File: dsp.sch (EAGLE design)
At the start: 128 parts, among them IC1 OPA2134P, IC2 OPA2134P, IC3 OPA2134P, U1 STM32F405RGT6, U2 CODECODER-WM8731SEDS/V(SSOP28), U4 LM2575HVS-3.3/NOPB, X1 ABLS-8.000MHZ-B4-T

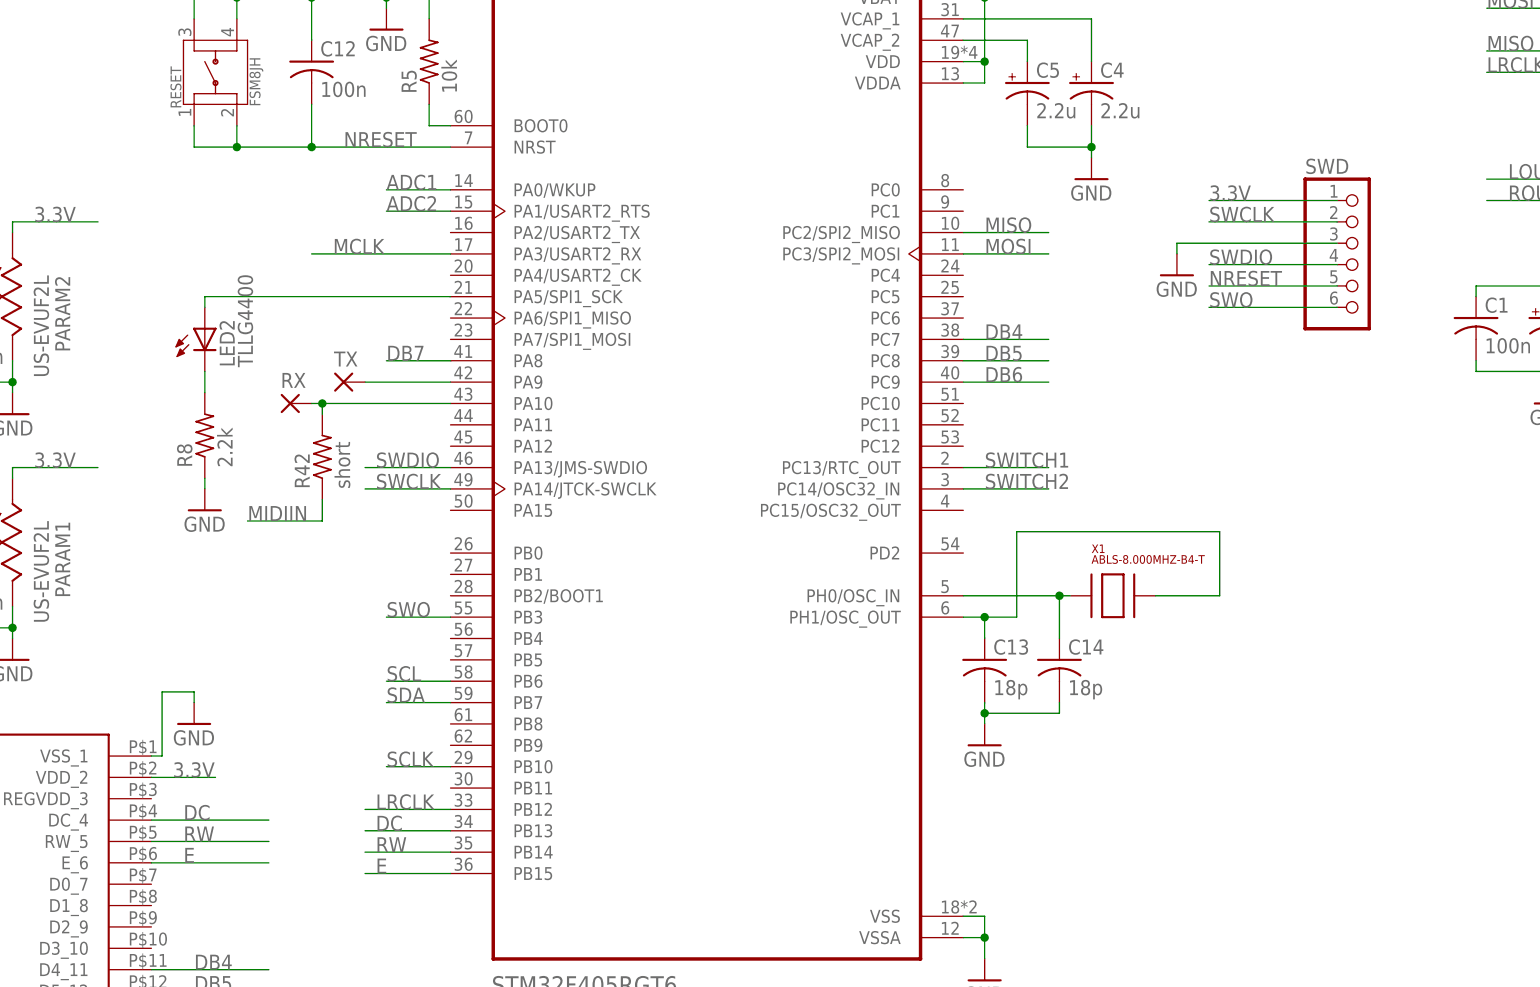
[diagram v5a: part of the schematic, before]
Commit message: added a ground for vccref and moved icp header to edge
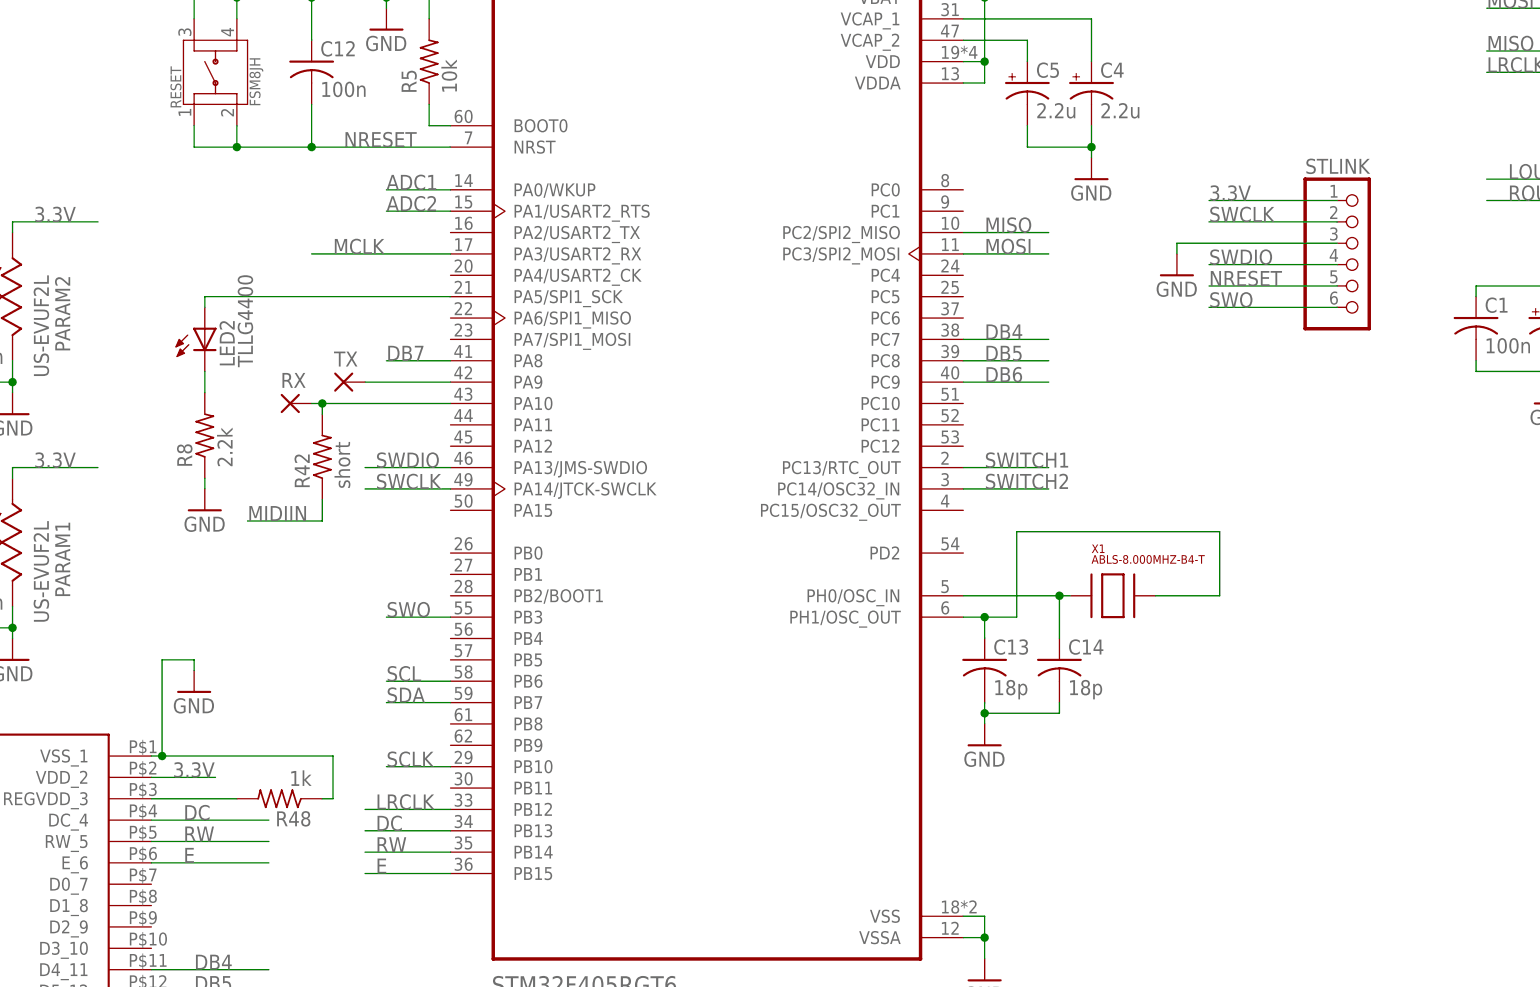
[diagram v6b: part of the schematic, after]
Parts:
- added R48: 1k, dan:R-US_0309/V
- renumbered SWD to STLINK
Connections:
- new net N$59: R48.2, U$1.REGVDD_3
- net GND: now also R48.1
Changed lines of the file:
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@@
 <part name="C28" library="dan" deviceset="C-US" device="050-025X075" value="180p"/>
 <part name="C29" library="dan" deviceset="C-US" device="050-025X075" value="180p"/>
-<part name="SWD" library="dan" deviceset="PINHD-1X6" device=""/>
+<part name="STLINK" library="dan" deviceset="PINHD-1X6" device=""/>
 <part name="RX" library="synthdiy" deviceset="2,0/0,9-S" device=""/>
 <part name="TX" library="synthdiy" deviceset="2,0/0,9-S" device=""/>
@@
 <part name="C37" library="dan" deviceset="CPOL-US" device="E2-4" value="1u"/>
 <part name="GND30" library="dan" deviceset="GND" device=""/>
+<part name="R48" library="dan" deviceset="R-US_" device="0309/V" value="1k"/>
 </parts>
 <sheets>
@@
 <instance part="R22" gate="G$1" x="99.06" y="212.09" rot="R90"/>
 <instance part="D4" gate="G$1" x="60.96" y="212.09" rot="R90"/>
-<instance part="GND35" gate="1" x="-7.62" y="10.16"/>
+<instance part="GND35" gate="1" x="-7.62" y="13.97"/>
 <instance part="GND36" gate="1" x="3.81" y="-33.02"/>
 <instance part="GND37" gate="1" x="-11.43" y="-45.72"/>
@@
 <instance part="C28" gate="G$1" x="295.91" y="118.11" rot="R90"/>
 <instance part="C29" gate="G$1" x="293.37" y="181.61" rot="R90"/>
-<instance part="SWD" gate="A" x="130.81" y="64.77"/>
+<instance part="STLINK" gate="A" x="130.81" y="64.77"/>
 <instance part="RX" gate="P" x="3.81" y="48.26"/>
 <instance part="TX" gate="P" x="10.16" y="50.8"/>
@@
 <instance part="C37" gate="G$1" x="209.55" y="67.31"/>
 <instance part="GND30" gate="1" x="203.2" y="83.82"/>
+<instance part="R48" gate="G$1" x="2.54" y="1.27" rot="R180"/>
 </instances>
 <busses>
@@
 <wire x1="109.22" y1="67.31" x2="109.22" y2="66.04" width="0.1524" layer="91"/>
 <pinref part="GND26" gate="1" pin="GND"/>
-<pinref part="SWD" gate="A" pin="3"/>
+<pinref part="STLINK" gate="A" pin="3"/>
 </segment>
 <segment>
@@
 <pinref part="U$1" gate="G$1" pin="VSS_1"/>
 <wire x1="-12.7" y1="6.35" x2="-11.43" y2="6.35" width="0.1524" layer="91"/>
-<wire x1="-11.43" y1="6.35" x2="-11.43" y2="13.97" width="0.1524" layer="91"/>
+<wire x1="-11.43" y1="6.35" x2="-11.43" y2="17.78" width="0.1524" layer="91"/>
 <pinref part="GND35" gate="1" pin="GND"/>
-<wire x1="-11.43" y1="13.97" x2="-7.62" y2="13.97" width="0.1524" layer="91"/>
-<wire x1="-7.62" y1="13.97" x2="-7.62" y2="12.7" width="0.1524" layer="91"/>
+<wire x1="-11.43" y1="17.78" x2="-7.62" y2="17.78" width="0.1524" layer="91"/>
+<wire x1="-7.62" y1="17.78" x2="-7.62" y2="16.51" width="0.1524" layer="91"/>
+<pinref part="R48" gate="G$1" pin="1"/>
+<wire x1="7.62" y1="1.27" x2="8.89" y2="1.27" width="0.1524" layer="91"/>
+<wire x1="8.89" y1="1.27" x2="8.89" y2="6.35" width="0.1524" layer="91"/>
+<wire x1="8.89" y1="6.35" x2="-11.43" y2="6.35" width="0.1524" layer="91"/>
+<junction x="-11.43" y="6.35"/>
 </segment>
 <segment>
@@
 </segment>
 <segment>
-<pinref part="SWD" gate="A" pin="1"/>
+<pinref part="STLINK" gate="A" pin="1"/>
 <wire x1="128.27" y1="72.39" x2="113.03" y2="72.39" width="0.1524" layer="91"/>
 <label x="113.03" y="72.39" size="1.778" layer="95"/>
@@
 </segment>
 <segment>
-<pinref part="SWD" gate="A" pin="5"/>
+<pinref part="STLINK" gate="A" pin="5"/>
 <wire x1="128.27" y1="62.23" x2="113.03" y2="62.23" width="0.1524" layer="91"/>
 <label x="113.03" y="62.23" size="1.778" layer="95"/>
@@
 </segment>
 <segment>
-<pinref part="SWD" gate="A" pin="2"/>
+<pinref part="STLINK" gate="A" pin="2"/>
 <wire x1="128.27" y1="69.85" x2="113.03" y2="69.85" width="0.1524" layer="91"/>
 <label x="113.03" y="69.85" size="1.778" layer="95"/>
@@
 </segment>
 <segment>
-<pinref part="SWD" gate="A" pin="4"/>
+<pinref part="STLINK" gate="A" pin="4"/>
 <wire x1="128.27" y1="64.77" x2="113.03" y2="64.77" width="0.1524" layer="91"/>
 <label x="113.03" y="64.77" size="1.778" layer="95"/>
@@
 </segment>
 <segment>
-<pinref part="SWD" gate="A" pin="6"/>
+<pinref part="STLINK" gate="A" pin="6"/>
 <wire x1="128.27" y1="59.69" x2="113.03" y2="59.69" width="0.1524" layer="91"/>
 <label x="113.03" y="59.69" size="1.778" layer="95"/>
@@
 </segment>
 </net>
+<net name="N$59" class="0">
+<segment>
+<pinref part="U$1" gate="G$1" pin="REGVDD_3"/>
+<pinref part="R48" gate="G$1" pin="2"/>
+<wire x1="-12.7" y1="1.27" x2="-2.54" y2="1.27" width="0.1524" layer="91"/>
+</segment>
+</net>

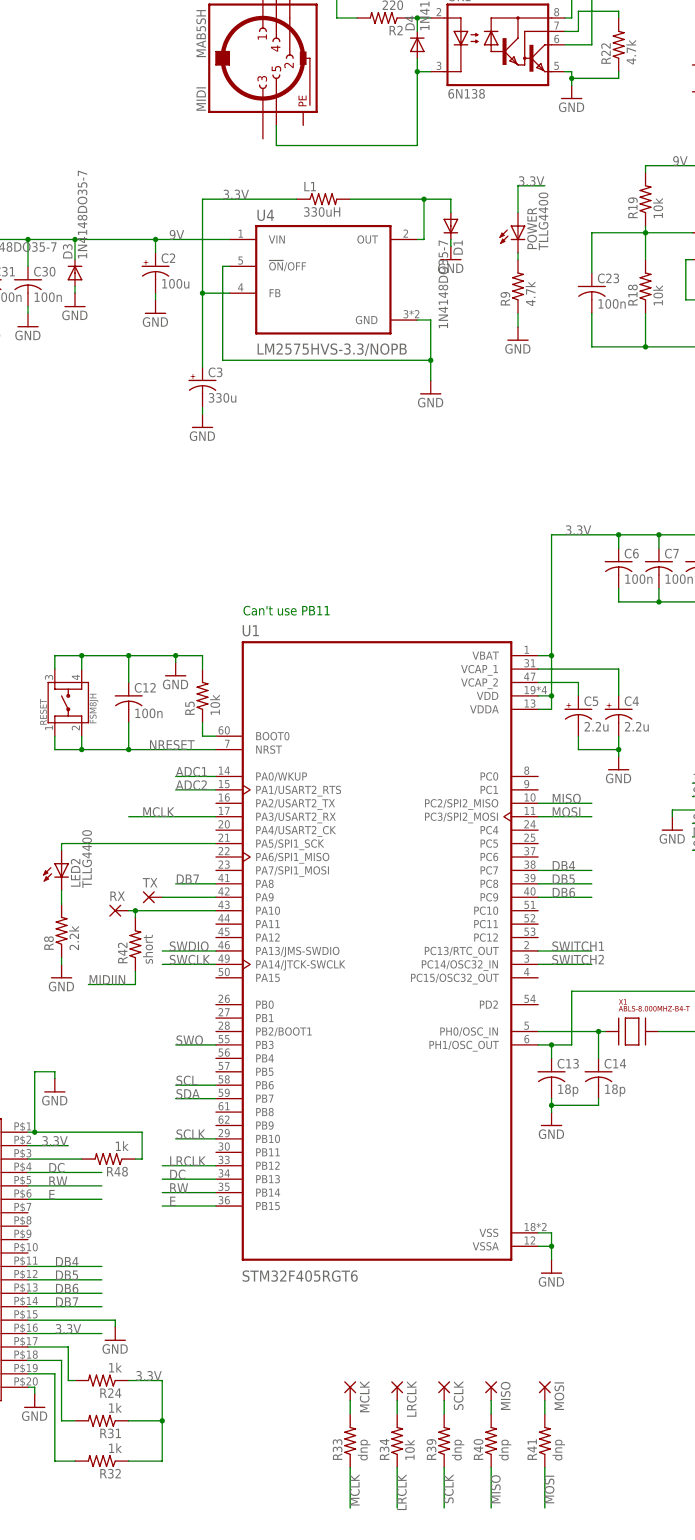
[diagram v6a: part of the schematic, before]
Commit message: added a mclk optin for pc6 for f405 compatibility
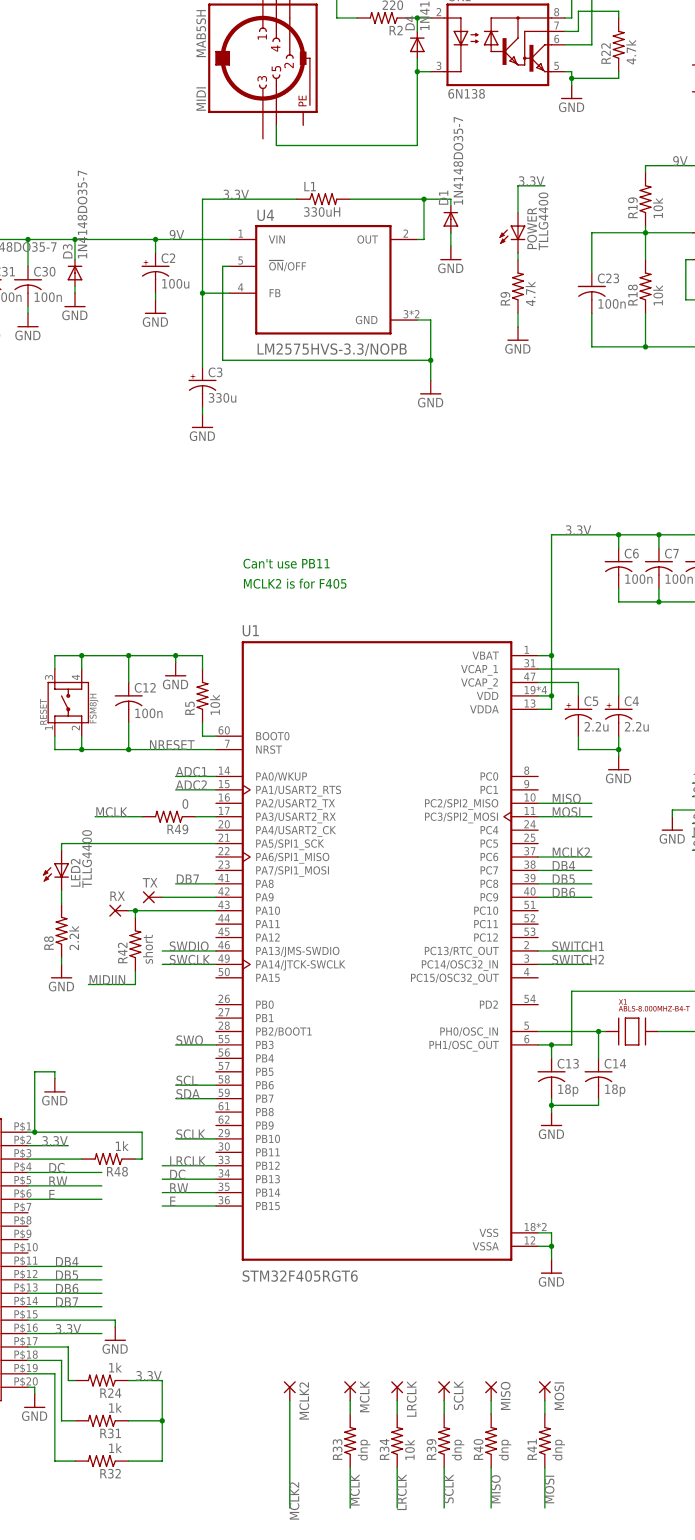
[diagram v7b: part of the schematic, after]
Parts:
- added MCLK2: (no value), synthdiy:2,0/0,9-S
- added R49: 0, dan:R-US_R0603
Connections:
- new net MCLK2: MCLK2.P, U1.PC6
- new net N$25: R49.1, U1.PA3/USART2_RX
- net GND: now also D1.A; no longer D1.C
- net MCLK: now also R49.2; no longer U1.PA3/USART2_RX
- net N$4: now also D1.C; no longer D1.A
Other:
- note added: "MCLK2 is for F405"
- moved on the sheet: D1
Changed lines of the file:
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@@
 <part name="GND30" library="dan" deviceset="GND" device=""/>
 <part name="R48" library="dan" deviceset="R-US_" device="0309/V" value="1k"/>
+<part name="MCLK2" library="synthdiy" deviceset="2,0/0,9-S" device=""/>
+<part name="R49" library="dan" deviceset="R-US_" device="R0603" value="0"/>
 </parts>
 <sheets>
 <sheet>
 <plain>
-<text x="27.94" y="104.14" size="1.778" layer="91">Can't use PB11</text>
+<text x="27.94" y="113.03" size="1.778" layer="91">Can't use PB11</text>
+<text x="27.94" y="109.22" size="1.778" layer="91">MCLK2 is for F405 </text>
 </plain>
 <instances>
@@
 <instance part="U$2" gate="G$2" x="-52.07" y="186.69"/>
 <instance part="U4" gate="A" x="43.18" y="167.64"/>
-<instance part="D1" gate="G$1" x="67.31" y="177.8" rot="R270"/>
+<instance part="D1" gate="G$1" x="67.31" y="179.07" rot="R90"/>
 <instance part="GND31" gate="1" x="67.31" y="171.45"/>
 <instance part="GND32" gate="1" x="80.01" y="156.21"/>
@@
 <instance part="GND30" gate="1" x="203.2" y="83.82"/>
 <instance part="R48" gate="G$1" x="2.54" y="1.27" rot="R180"/>
+<instance part="MCLK2" gate="P" x="36.83" y="-41.91" rot="R270"/>
+<instance part="R49" gate="G$1" x="13.97" y="66.04" rot="R180"/>
 </instances>
 <busses>
@@
 </segment>
 <segment>
-<pinref part="D1" gate="G$1" pin="C"/>
-<pinref part="GND31" gate="1" pin="GND"/>
-<wire x1="67.31" y1="175.26" x2="67.31" y2="173.99" width="0.1524" layer="91"/>
-</segment>
-<segment>
 <pinref part="GND5" gate="1" pin="GND"/>
 <pinref part="C3" gate="G$1" pin="-"/>
@@
 <wire x1="203.2" y1="87.63" x2="199.39" y2="87.63" width="0.1524" layer="91"/>
 <junction x="199.39" y="87.63"/>
+</segment>
+<segment>
+<pinref part="GND31" gate="1" pin="GND"/>
+<pinref part="D1" gate="G$1" pin="A"/>
+<wire x1="67.31" y1="173.99" x2="67.31" y2="176.53" width="0.1524" layer="91"/>
 </segment>
 </net>
@@
 </segment>
 <segment>
-<pinref part="U1" gate="G$1" pin="PA3/USART2_RX"/>
-<wire x1="22.86" y1="66.04" x2="6.35" y2="66.04" width="0.1524" layer="91"/>
-<label x="8.89" y="66.04" size="1.778" layer="95"/>
+<pinref part="R49" gate="G$1" pin="2"/>
+<wire x1="8.89" y1="66.04" x2="0" y2="66.04" width="0.1524" layer="91"/>
+<label x="0" y="66.04" size="1.778" layer="95"/>
 </segment>
 </net>
@@
 <pinref part="L1" gate="G$1" pin="2"/>
 <wire x1="62.23" y1="182.88" x2="48.26" y2="182.88" width="0.1524" layer="91"/>
-<pinref part="D1" gate="G$1" pin="A"/>
-<wire x1="67.31" y1="180.34" x2="67.31" y2="182.88" width="0.1524" layer="91"/>
 <wire x1="67.31" y1="182.88" x2="62.23" y2="182.88" width="0.1524" layer="91"/>
 <junction x="62.23" y="182.88"/>
+<pinref part="D1" gate="G$1" pin="C"/>
+<wire x1="67.31" y1="181.61" x2="67.31" y2="182.88" width="0.1524" layer="91"/>
 </segment>
 </net>
@@
 </segment>
 </net>
+<net name="MCLK2" class="0">
+<segment>
+<label x="36.83" y="-59.69" size="1.778" layer="95" rot="R270"/>
+<pinref part="MCLK2" gate="P" pin="P"/>
+<wire x1="36.83" y1="-64.77" x2="36.83" y2="-44.45" width="0.1524" layer="91"/>
+</segment>
+<segment>
+<wire x1="83.82" y1="58.42" x2="93.98" y2="58.42" width="0.1524" layer="91"/>
+<label x="86.36" y="58.42" size="1.778" layer="95"/>
+<pinref part="U1" gate="G$1" pin="PC6"/>
+</segment>
+</net>
+<net name="N$25" class="0">
+<segment>
+<pinref part="U1" gate="G$1" pin="PA3/USART2_RX"/>
+<pinref part="R49" gate="G$1" pin="1"/>
+<wire x1="19.05" y1="66.04" x2="22.86" y2="66.04" width="0.1524" layer="91"/>
+</segment>
+</net>

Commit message: sent it out to get made
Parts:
- removed LED2: TLLG4400, dan:TLLG4400
- added LED1: (no value), dan:LED5MM
- POWER: value TLLG4400 -> (none); device dan:TLLG4400 -> dan:LED5MM
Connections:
- new net N$60: IC3B.-IN, IC3B.OUT
- net 3.3V: now also U2.HPVDD
- net GND: now also IC3B.+IN, U2.HPGND
- net N$10: now also LED1.C; no longer LED2.C
- net N$9: now also LED1.A; no longer LED2.A
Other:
- moved on the sheet: POWER
